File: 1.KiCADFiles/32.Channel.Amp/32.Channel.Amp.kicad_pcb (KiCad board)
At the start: 4 copper layers, 335.2 x 204.1 mm, 5 parts

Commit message: Updated 32 Channel Format, Included Chip Board
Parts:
- removed the REF** at (350.2, 195.7)
- removed the REF** at (350.2, 225.7)
- removed the REF** at (23.5, 64.1)
- removed the REF** at (39.6, 89.0)
- added C1: 10uF, Capacitor_SMD:C_1206_3216Metric_Pad1.33x1.80mm_HandSolder, B.Cu at (96.5, 87.2)
- added C2: 10uF, Capacitor_SMD:C_1206_3216Metric_Pad1.33x1.80mm_HandSolder, B.Cu at (106.3, 91.2)
- added C3: 10uF, Capacitor_SMD:C_1206_3216Metric_Pad1.33x1.80mm_HandSolder, F.Cu at (95.4, 102.7)
- added C4: 10uF, Capacitor_SMD:C_1206_3216Metric_Pad1.33x1.80mm_HandSolder, F.Cu at (105.6, 98.9)
- added D1: 1N4148W, Diode_SMD:D_SOD-123, B.Cu at (96.6, 84.1)
- added D2: 1N4148W, Diode_SMD:D_SOD-123, B.Cu at (105.8, 88.5)
- added D3: BZV55B7V5, Diode_SMD:D_MiniMELF, B.Cu at (100.9, 88.5)
- added D4: BZV55B7V5, Diode_SMD:D_MiniMELF, B.Cu at (107.0, 103.0)
- added J4: Conn_01x08, Connector_PinSocket_2.54mm:PinSocket_1x08_P2.54mm_Vertical, F.Cu at (100.5, 94.5)
- added Q1: MMBT3904, Package_TO_SOT_SMD:SOT-23, B.Cu at (95.9, 93.2)
- added Q2: MMBT3906, Package_TO_SOT_SMD:SOT-23, B.Cu at (104.6, 98.3)
- added R1: 1.0k, Resistor_SMD:R_1206_3216Metric_Pad1.30x1.75mm_HandSolder, B.Cu at (96.5, 89.9)
- added R2: 1.0k, Resistor_SMD:R_1206_3216Metric_Pad1.30x1.75mm_HandSolder, B.Cu at (106.2, 94.1)
- added R3: 4.7, Resistor_SMD:R_1206_3216Metric_Pad1.30x1.75mm_HandSolder, F.Cu at (104.0, 103.5)
- added R4: 4.7, Resistor_SMD:R_1206_3216Metric_Pad1.30x1.75mm_HandSolder, F.Cu at (97.0, 98.2)
- added REF**: DSUB-9_Female_Horizontal_P2.77x2.54mm_EdgePinOffset9.40mm, Connector_Dsub:DSUB-9_Female_Horizontal_P2.77x2.54mm_EdgePinOffset9.40mm, F.Cu at (240.6, 165.3)
- added REF**: CONN D-SUB PLUG 50POS RA SLDR, 1.Local.Library:CONN D-SUB PLUG 50POS RA SLDR, F.Cu at (180.0, 172.0)
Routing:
- net (no net): track 156.3 -> 28.6 mm, vias 32 -> 20
- net Net-(J2-In): track 0.00 -> 15.6 mm
- net Net-(D4-A): track 0.00 -> 12.3 mm
- net +11: track 0.00 -> 11.0 mm
- net -11: track 0.00 -> 10.4 mm
- net Net-(D1-A): track 0.00 -> 9.30 mm
- net Net-(D3-K): track 0.00 -> 8.85 mm
- net Net-(J3-In): track 0.00 -> 8.21 mm
- net GND: track 0.00 -> 4.00 mm, vias 0 -> 1
- net Net-(D2-K): track 0.00 -> 1.59 mm
- net GND1: vias 0 -> 1
- added copper zone on B.Cu, net (none)
- added copper zone on F.Cu, net (none)
- added copper zone on In1.Cu, net (none)
- added copper zone on In2.Cu, net (none)
- added copper zone on B.Cu, net GND
- added copper zone on In2.Cu, net GND
- added copper zone on F.Cu, net GND1
- added copper zone on In1.Cu, net GND1
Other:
- board size 335.2 x 204.1 mm -> 164.5 x 130 mm
- board text added: "June 2023 Alfredo Barajas Enriquez"
- board text added: "in"
- board text added: "out"

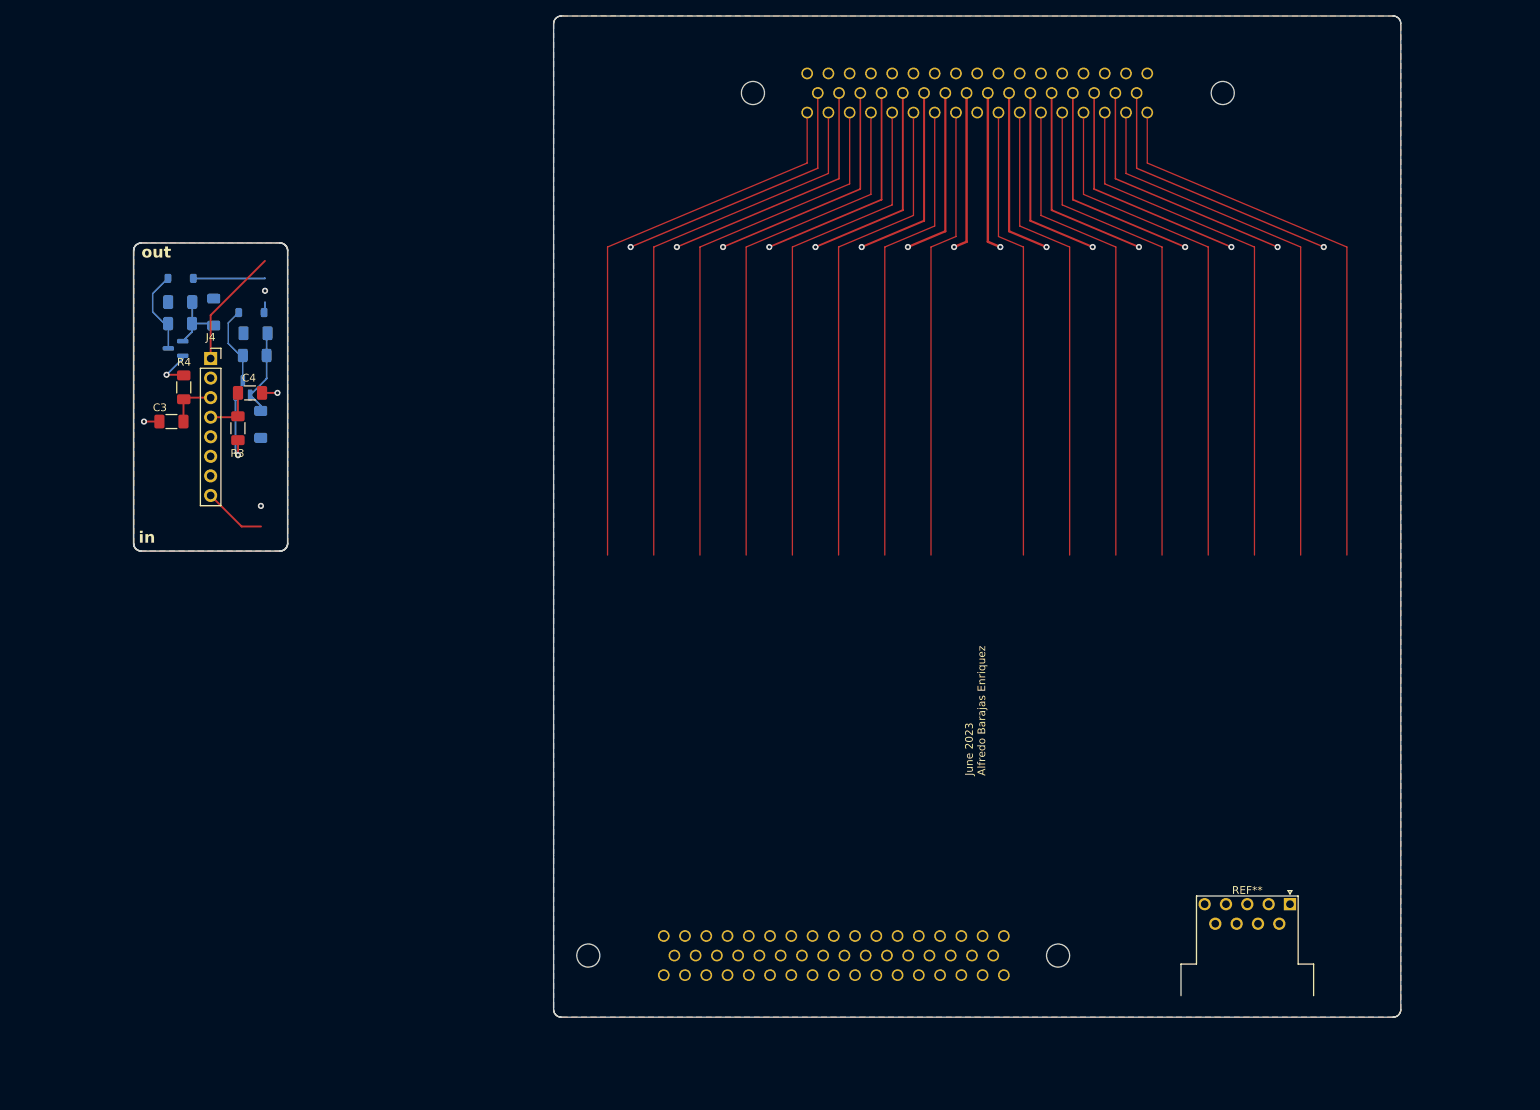
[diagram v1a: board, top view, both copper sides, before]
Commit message: Created two 32 Channel Boards. Adjusted traces for capacitance
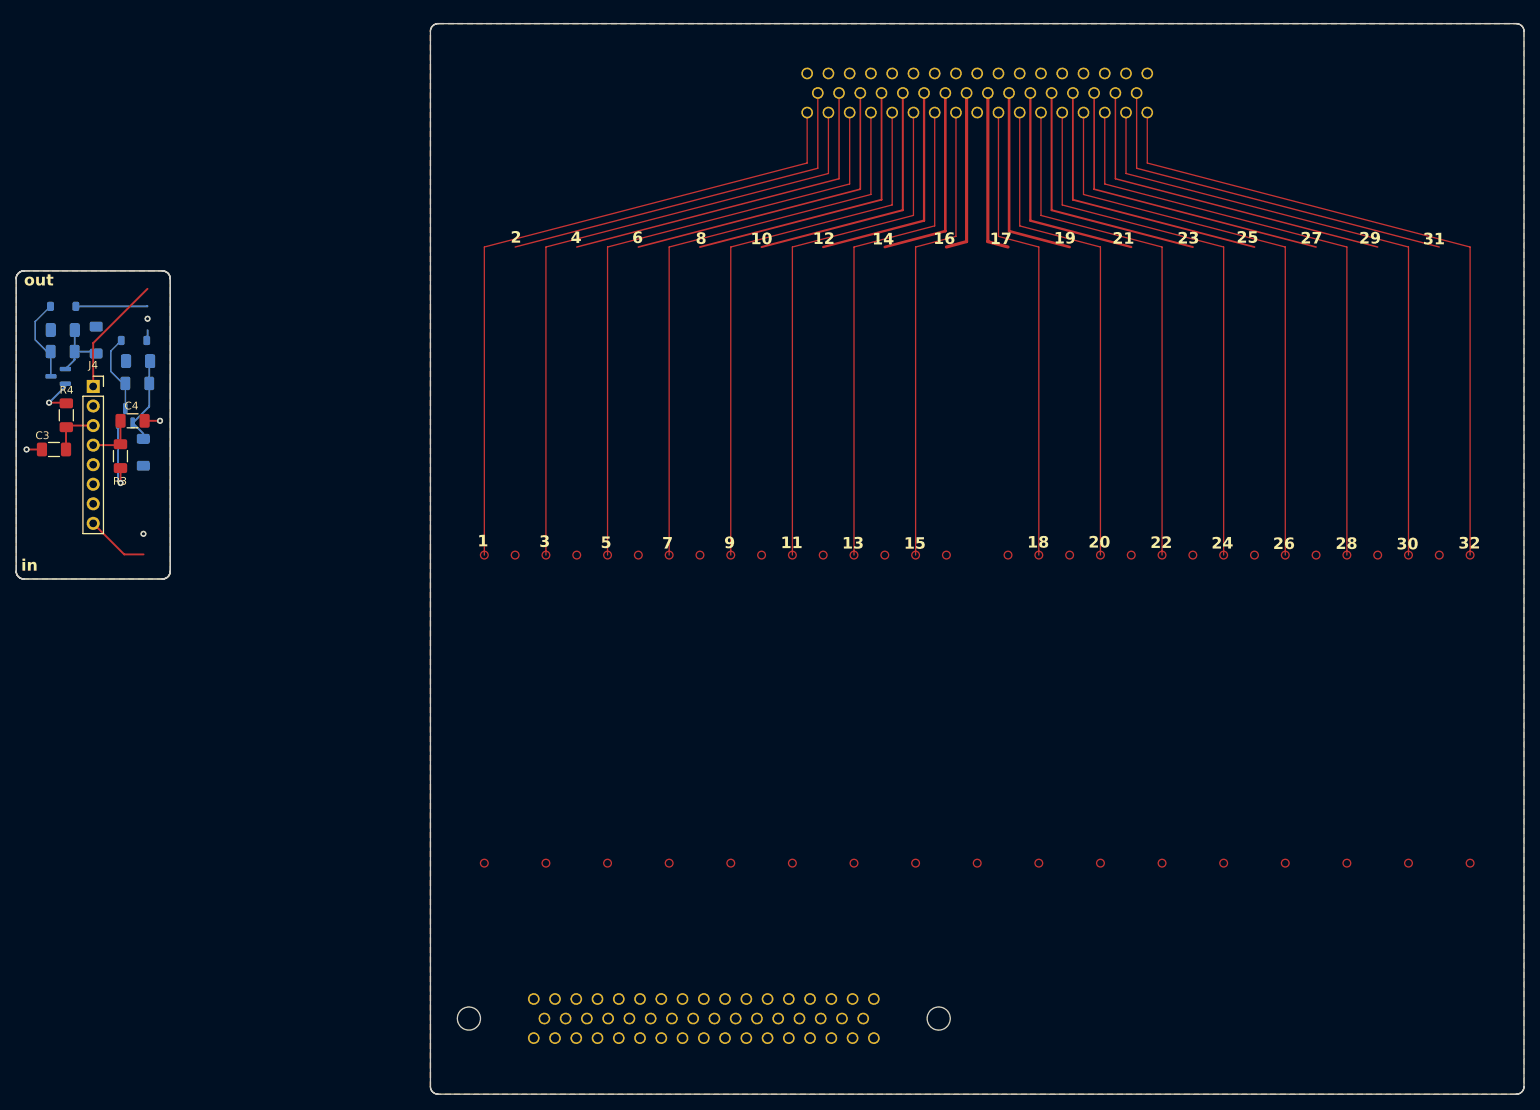
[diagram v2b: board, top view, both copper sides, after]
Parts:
- removed the REF** at (240.6, 165.3)
- moved REF** 18.8 mm to (163.1, 180.2)
- moved C1 15.7 mm to (81.3, 90.8)
- moved C2 15.7 mm to (91.0, 94.8)
- moved Q1 15.7 mm to (80.7, 96.8)
- moved R3 15.7 mm to (88.8, 107.2)
- moved R4 15.7 mm to (81.7, 101.8)
- moved D2 15.7 mm to (90.5, 92.1)
- moved J4 15.7 mm to (85.2, 98.1)
- moved Q2 15.7 mm to (89.4, 101.9)
- moved R1 15.7 mm to (81.2, 93.6)
- moved C4 15.7 mm to (90.3, 102.6)
- moved D3 15.7 mm to (85.6, 92.1)
- moved D4 15.7 mm to (91.7, 106.7)
- moved R2 15.7 mm to (90.9, 97.7)
- moved C3 15.7 mm to (80.1, 106.3)
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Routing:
- net (no net): vias 20 -> 4
- removed copper zone on B.Cu, net (none)
- removed copper zone on F.Cu, net (none)
- removed copper zone on In1.Cu, net (none)
- removed copper zone on In2.Cu, net (none)
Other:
- board size 164.5 x 130 mm -> 195.8 x 139 mm
- board text added: "1"
- board text added: "10"
- board text added: "11"
- board text added: "12"
- board text added: "13"
- board text added: "14"
- board text added: "15"
- board text added: "16"
- board text added: "17"
- board text added: "18"
- board text added: "19"
- board text added: "2"
- board text added: "20"
- board text added: "21"
- board text added: "22"
- board text added: "23"
- board text added: "24"
- board text added: "25"
- board text added: "26"
- board text added: "27"
- board text added: "28"
- board text added: "29"
- board text added: "3"
- board text added: "30"
- board text added: "31"
- board text added: "32"
- board text added: "4"
- board text added: "5"
- board text added: "6"
- board text added: "7"
- board text added: "8"
- board text added: "9"
- board text removed: "June 2023 Alfredo Barajas Enriquez"

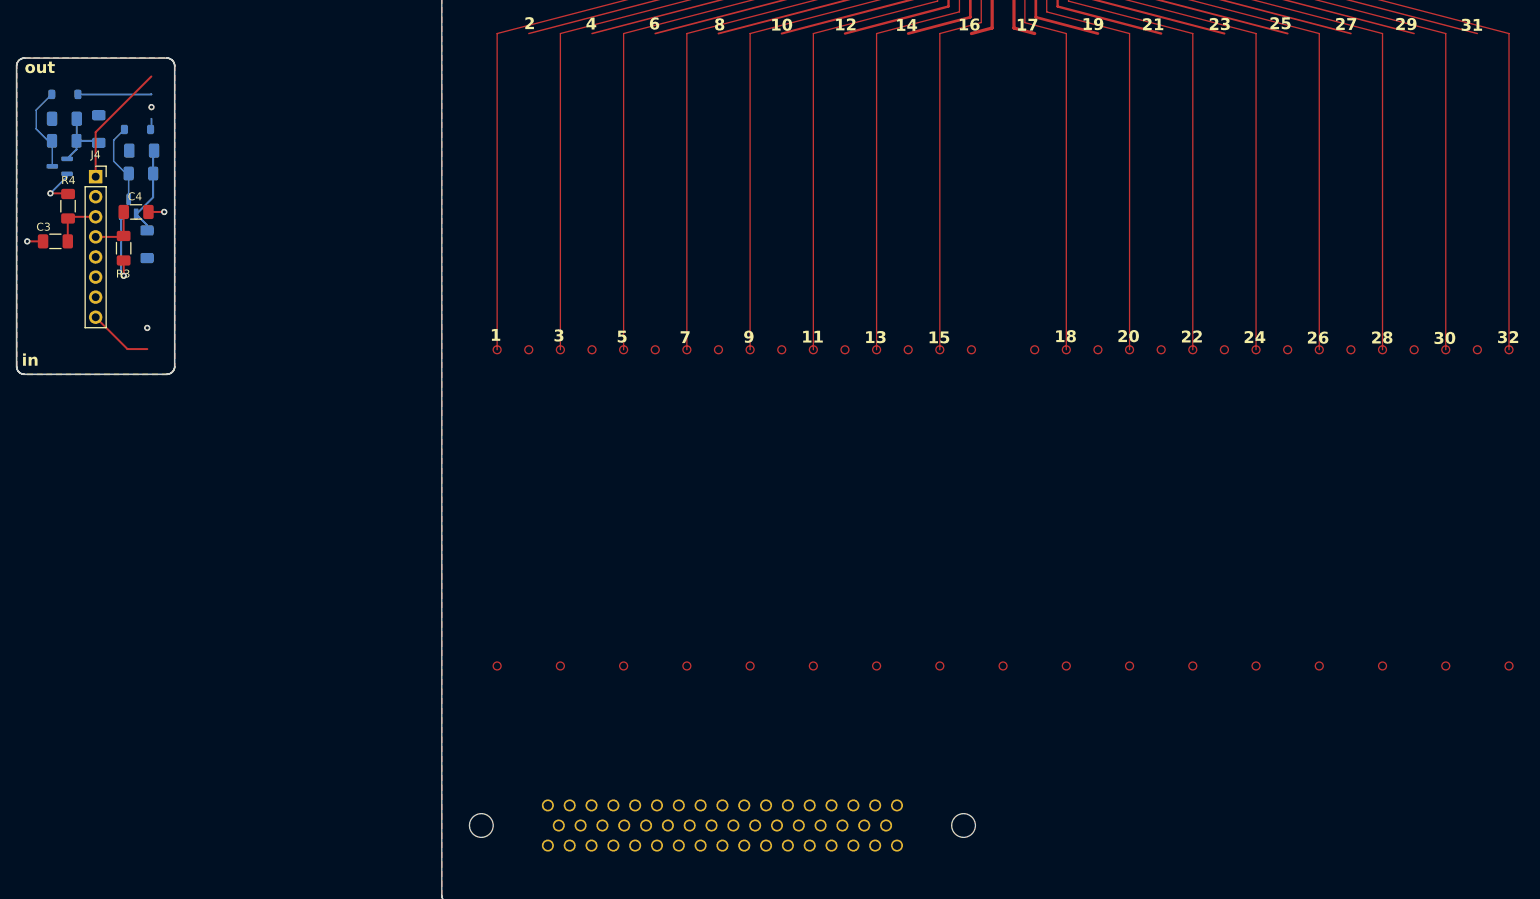
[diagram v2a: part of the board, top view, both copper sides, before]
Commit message: Added Amp Cell for 32 Channel Board
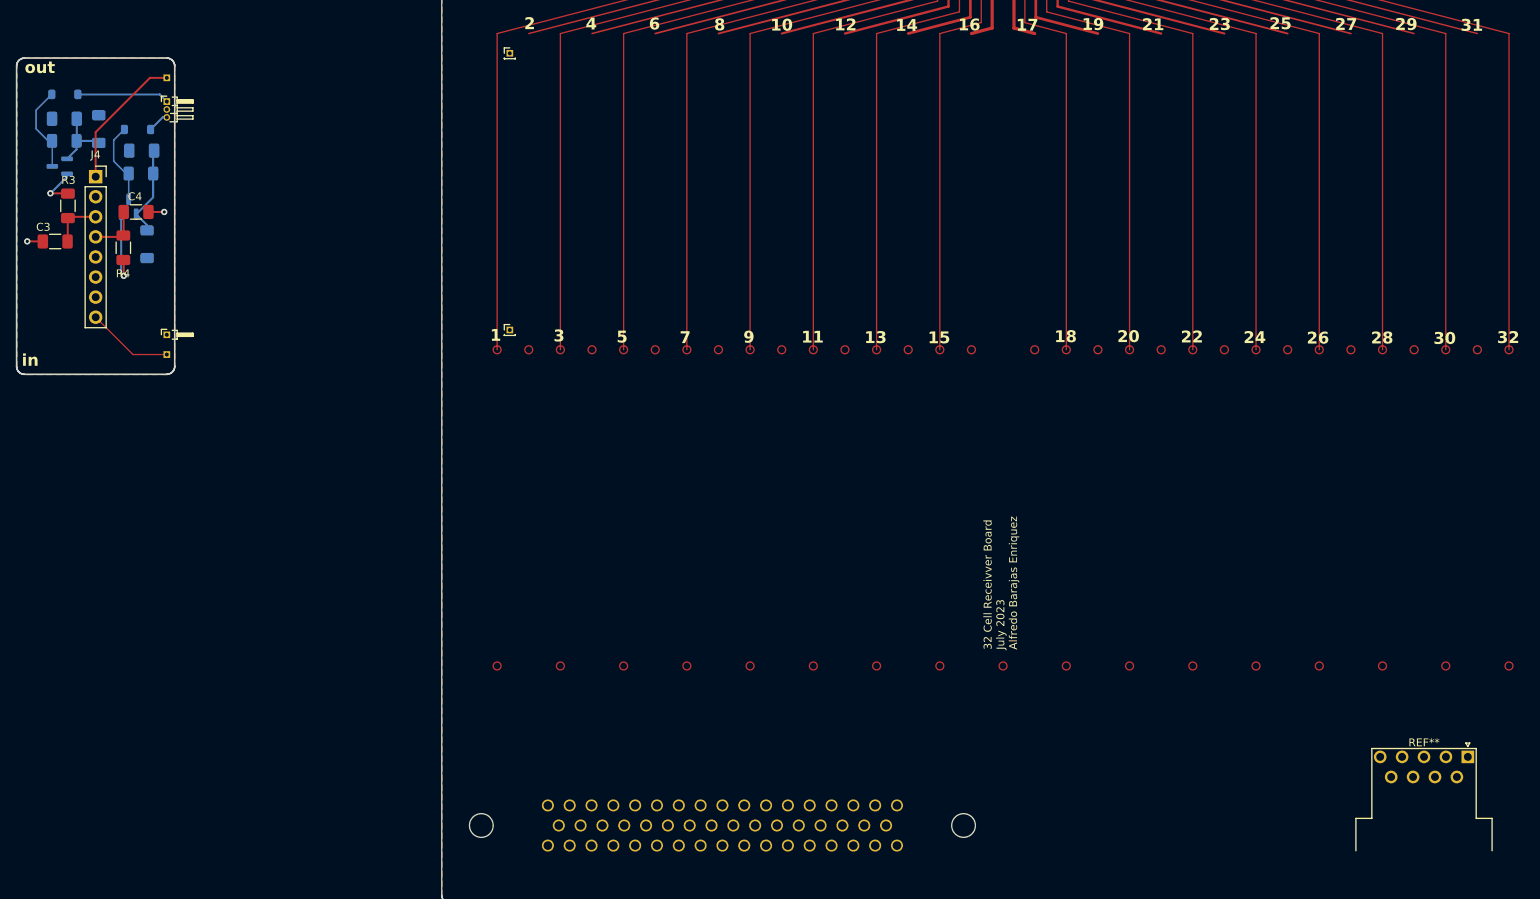
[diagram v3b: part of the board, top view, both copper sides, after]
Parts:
- added REF**: PinHeader_1x01_P1.00mm_Vertical, Connector_PinHeader_1.00mm:PinHeader_1x01_P1.00mm_Vertical, F.Cu at (137.6, 117.5)
- added REF**: DSUB-9_Female_Horizontal_P2.77x2.54mm_EdgePinOffset9.40mm, Connector_Dsub:DSUB-9_Female_Horizontal_P2.77x2.54mm_EdgePinOffset9.40mm, F.Cu at (258.8, 171.5)
- added REF**: PinHeader_1x01_P1.00mm_Vertical, Connector_PinHeader_1.00mm:PinHeader_1x01_P1.00mm_Vertical, F.Cu at (137.6, 82.5)
- added REF**: PinHeader_1x01_P1.00mm_Horizontal, Connector_PinHeader_1.00mm:PinHeader_1x01_P1.00mm_Horizontal, F.Cu at (94.2, 118.1)
- added REF**: PinHeader_1x03_P1.00mm_Horizontal, Connector_PinHeader_1.00mm:PinHeader_1x03_P1.00mm_Horizontal, F.Cu at (94.2, 88.6)
- added REF**: PinHeader_1x01_P1.00mm_Horizontal, Connector_PinHeader_1.00mm:PinHeader_1x01_P1.00mm_Horizontal, B.Cu at (94.2, 85.6)
- added REF**: PinHeader_1x01_P1.00mm_Horizontal, Connector_PinHeader_1.00mm:PinHeader_1x01_P1.00mm_Horizontal, B.Cu at (94.2, 120.6)
- moved R3 8.85 mm to (81.7, 101.8), turned to -90 degrees
- moved R4 8.74 mm to (88.7, 107.1), turned to 90 degrees
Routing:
- net (no net): track 28.6 -> 0.00 mm, vias 4 -> 2
- net Net-(Q2-E): track 0.00 -> 9.88 mm
- net Net-(J4-Pin_4): track 0.00 -> 6.66 mm
- net Net-(J4-Pin_3): track 0.00 -> 6.49 mm
- net Net-(Q1-E): track 0.00 -> 5.61 mm
- net Net-(J3-In): track 8.21 -> 11.0 mm
- net Net-(D1-A): track 9.30 -> 11.6 mm
- net Net-(J2-In): track 15.6 -> 17.5 mm
- net Net-(D2-K): track 1.59 -> 2.88 mm
- net GND1: vias 1 -> 0
- net GND: vias 1 -> 2
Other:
- board text added: "32 Cell Receivver Board July 2023 Alfredo Barajas Enriquez"
